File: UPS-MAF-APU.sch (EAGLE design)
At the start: 3 parts, among them J1 CONNECTOR_PI_40_PIN, J3 CONNECTOR_4, U1 OLED_I2C

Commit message: add more to-do items for schematic
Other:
- note added: "add battery/charger connector add INA260 add JST-4 for console add galvanic isolator add 1x6 for FTDI? add RJ-45 magjack add ENC28J60 eth IC package SS add power LED add OKI 78SR 5V SMPS add external temp connector add Si7006 internal temp/humidity add power, status lights"
- note removed: "add battery/charger connector add INA260 add JST-4 for console add 1x6 for FTDI? add RJ-45 magjack add ENC28J60 eth IC package SS add power LED add OKI 78SR 5V SMPS"
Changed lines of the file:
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@@
 add INA260
 add JST-4 for console
+add galvanic isolator
 add 1x6 for FTDI?
 add RJ-45 magjack
 add ENC28J60 eth IC package SS
 add power LED
-add OKI 78SR 5V SMPS</text>
+add OKI 78SR 5V SMPS
+add external temp connector
+add Si7006 internal temp/humidity
+add power, status lights</text>
 </plain>
 <instances>

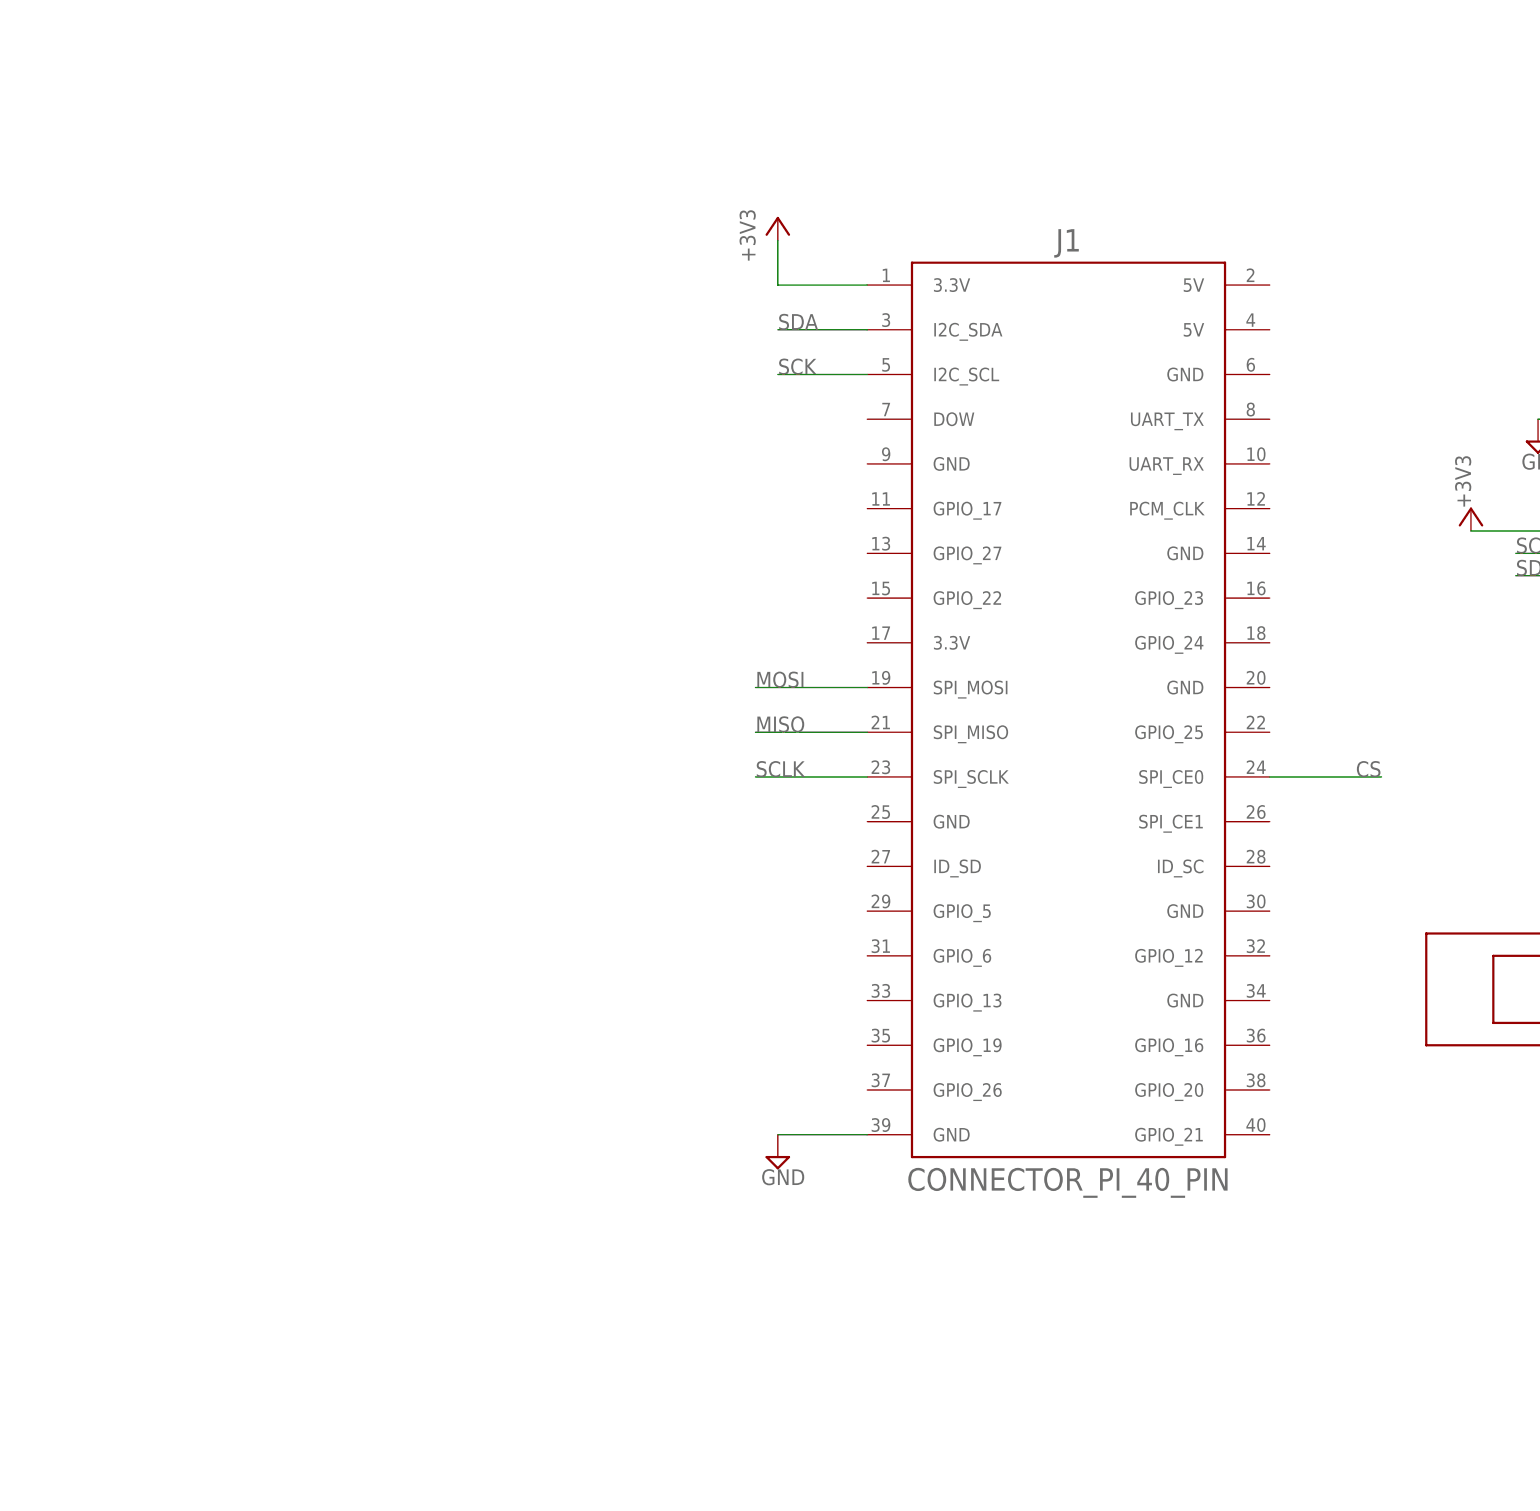
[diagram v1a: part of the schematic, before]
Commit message: Add parts to library, Schematic. Add barrel power jack, INA260 I/V sensor, 5V Murata SMPS.  Change parts to UPS library.
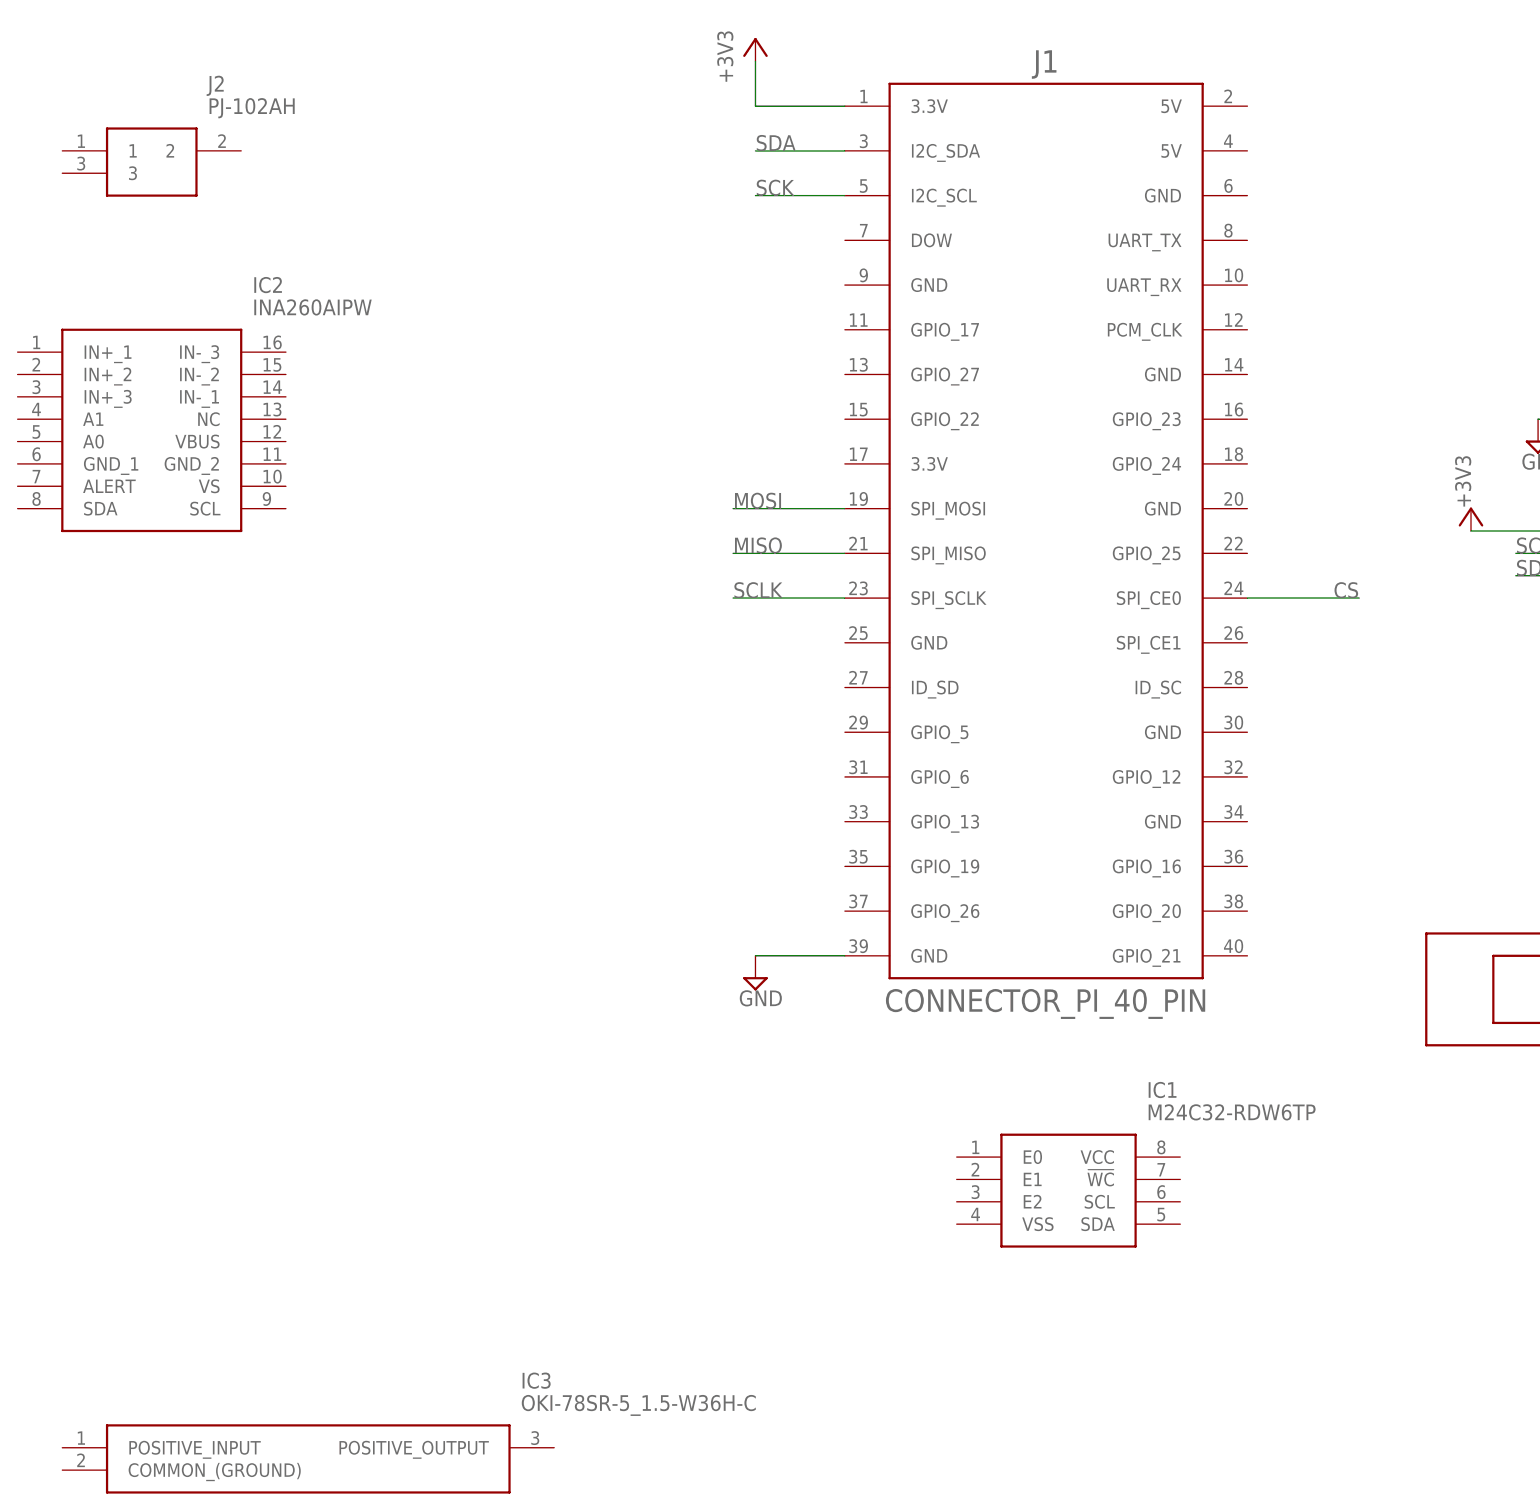
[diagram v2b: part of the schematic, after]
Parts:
- added IC1: M24C32-RDW6TP, APU_ENGR480_UPS_EAGLE_Library:M24C32-RDW6TP
- added IC2: INA260AIPW, APU_ENGR480_UPS_EAGLE_Library:INA260AIPW
- added IC3: OKI-78SR-5_1.5-W36H-C, APU_ENGR480_UPS_EAGLE_Library:OKI-78SR-5_1.5-W36H-C
- added J2: PJ-102AH, APU_ENGR480_UPS_EAGLE_Library:PJ-102AH
- J1: device ConnectBox_2019:CONNECTOR_PI_40_PIN -> APU_ENGR480_UPS_EAGLE_Library:CONNECTOR_PI_40_PIN
- J3: device ConnectBox_2019:CONNECTOR_4 -> APU_ENGR480_UPS_EAGLE_Library:CONNECTOR_4
- U1: device ConnectBox_2019:OLED_I2C -> APU_ENGR480_UPS_EAGLE_Library:OLED_I2C
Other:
- note added: "add battery/charger connector add JST-4 for console add galvanic isolator add 1x6 for FTDI? add RJ-45 magjack add power LED add external temp connector add Si7006 internal temp/humidity add power, status lights"
- note removed: "add battery/charger connector add INA260 add JST-4 for console add galvanic isolator add 1x6 for FTDI? add RJ-45 magjack add ENC28J60 eth IC package SS add power LED add OKI 78SR 5V SMPS add external temp connector add Si7006 internal temp/humidity add power, status lights"
- moved on the sheet: J1
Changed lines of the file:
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@@
 </classes>
 <parts>
-<part name="FRAME1" library="ConnectBox_2019" deviceset="FRAMES_LETTER_L" device=""/>
-<part name="J1" library="ConnectBox_2019" deviceset="CONNECTOR_PI_40_PIN" device=""/>
-<part name="+3V1" library="ConnectBox_2019" deviceset="+3V3" device=""/>
-<part name="SUPPLY2" library="ConnectBox_2019" deviceset="GND" device=""/>
-<part name="U1" library="ConnectBox_2019" deviceset="OLED_I2C" device=""/>
-<part name="+3V3" library="ConnectBox_2019" deviceset="+3V3" device=""/>
-<part name="SUPPLY3" library="ConnectBox_2019" deviceset="GND" device=""/>
-<part name="J3" library="ConnectBox_2019" deviceset="CONNECTOR_4" device=""/>
+<part name="FRAME1" library="APU_ENGR480_UPS_EAGLE_Library" deviceset="FRAMES_LETTER_L" device=""/>
+<part name="J1" library="APU_ENGR480_UPS_EAGLE_Library" deviceset="CONNECTOR_PI_40_PIN" device=""/>
+<part name="+3V1" library="APU_ENGR480_UPS_EAGLE_Library" deviceset="+3V3" device=""/>
+<part name="SUPPLY2" library="APU_ENGR480_UPS_EAGLE_Library" deviceset="GND" device=""/>
+<part name="U1" library="APU_ENGR480_UPS_EAGLE_Library" deviceset="OLED_I2C" device=""/>
+<part name="+3V3" library="APU_ENGR480_UPS_EAGLE_Library" deviceset="+3V3" device=""/>
+<part name="SUPPLY3" library="APU_ENGR480_UPS_EAGLE_Library" deviceset="GND" device=""/>
+<part name="J3" library="APU_ENGR480_UPS_EAGLE_Library" deviceset="CONNECTOR_4" device=""/>
+<part name="IC1" library="APU_ENGR480_UPS_EAGLE_Library" deviceset="M24C32-RDW6TP" device=""/>
+<part name="IC2" library="APU_ENGR480_UPS_EAGLE_Library" deviceset="INA260AIPW" device=""/>
+<part name="IC3" library="APU_ENGR480_UPS_EAGLE_Library" deviceset="OKI-78SR-5_1.5-W36H-C" device=""/>
+<part name="J2" library="APU_ENGR480_UPS_EAGLE_Library" deviceset="PJ-102AH" device=""/>
 </parts>
 <sheets>
@@
 <plain>
 <text x="-2.54" y="185.42" size="3.81" layer="88" align="top-right">add battery/charger connector
-add INA260
 add JST-4 for console
 add galvanic isolator
 add 1x6 for FTDI?
 add RJ-45 magjack
-add ENC28J60 eth IC package SS
 add power LED
-add OKI 78SR 5V SMPS
 add external temp connector
 add Si7006 internal temp/humidity
@@
 <attribute name="DRAWING_NAME" x="165.1" y="19.05" size="2.54" layer="94"/>
 </instance>
-<instance part="J1" gate="G$1" x="147.32" y="101.6" smashed="yes">
-<attribute name="NAME" x="147.32" y="154.94" size="2.54" layer="95" align="center"/>
-<attribute name="VALUE" x="147.32" y="48.26" size="2.54" layer="96" align="center"/>
+<instance part="J1" gate="G$1" x="144.78" y="121.92" smashed="yes">
+<attribute name="NAME" x="144.78" y="175.26" size="2.54" layer="95" align="center"/>
+<attribute name="VALUE" x="144.78" y="68.58" size="2.54" layer="96" align="center"/>
 </instance>
-<instance part="+3V1" gate="G$1" x="114.3" y="157.48" smashed="yes">
-<attribute name="VALUE" x="111.76" y="152.4" size="1.778" layer="96" rot="R90"/>
+<instance part="+3V1" gate="G$1" x="111.76" y="177.8" smashed="yes">
+<attribute name="VALUE" x="109.22" y="172.72" size="1.778" layer="96" rot="R90"/>
 </instance>
-<instance part="SUPPLY2" gate="GND" x="114.3" y="50.8" smashed="yes">
-<attribute name="VALUE" x="112.395" y="47.625" size="1.778" layer="96"/>
+<instance part="SUPPLY2" gate="GND" x="111.76" y="71.12" smashed="yes">
+<attribute name="VALUE" x="109.855" y="67.945" size="1.778" layer="96"/>
 </instance>
 <instance part="U1" gate="G$1" x="213.36" y="71.12" smashed="yes">
@@
 <attribute name="NAME" x="218.44" y="129.54" size="2.0828" layer="95" rot="MR180" align="center"/>
 </instance>
+<instance part="IC1" gate="G$1" x="134.62" y="50.8" smashed="yes">
+<attribute name="NAME" x="156.21" y="58.42" size="1.778" layer="95" align="center-left"/>
+<attribute name="VALUE" x="156.21" y="55.88" size="1.778" layer="96" align="center-left"/>
+</instance>
+<instance part="IC2" gate="G$1" x="27.94" y="142.24" smashed="yes">
+<attribute name="NAME" x="54.61" y="149.86" size="1.778" layer="95" align="center-left"/>
+<attribute name="VALUE" x="54.61" y="147.32" size="1.778" layer="96" align="center-left"/>
+</instance>
+<instance part="IC3" gate="G$1" x="33.02" y="17.78" smashed="yes">
+<attribute name="NAME" x="85.09" y="25.4" size="1.778" layer="95" align="center-left"/>
+<attribute name="VALUE" x="85.09" y="22.86" size="1.778" layer="96" align="center-left"/>
+</instance>
+<instance part="J2" gate="G$1" x="33.02" y="165.1" smashed="yes">
+<attribute name="NAME" x="49.53" y="172.72" size="1.778" layer="95" align="center-left"/>
+<attribute name="VALUE" x="49.53" y="170.18" size="1.778" layer="96" align="center-left"/>
+</instance>
 </instances>
 <busses>
@@
 <segment>
 <pinref part="J1" gate="G$1" pin="SPI_CE0@24"/>
-<wire x1="182.88" y1="93.98" x2="170.18" y2="93.98" width="0.1524" layer="91"/>
-<label x="182.88" y="93.98" size="1.778" layer="95" rot="MR0"/>
+<wire x1="180.34" y1="114.3" x2="167.64" y2="114.3" width="0.1524" layer="91"/>
+<label x="180.34" y="114.3" size="1.778" layer="95" rot="MR0"/>
 </segment>
 </net>
@@
 <segment>
 <pinref part="J1" gate="G$1" pin="SPI_MOSI@19"/>
-<wire x1="111.76" y1="104.14" x2="124.46" y2="104.14" width="0.1524" layer="91"/>
-<label x="111.76" y="104.14" size="1.778" layer="95"/>
+<wire x1="109.22" y1="124.46" x2="121.92" y2="124.46" width="0.1524" layer="91"/>
+<label x="109.22" y="124.46" size="1.778" layer="95"/>
 </segment>
 </net>
@@
 <pinref part="J1" gate="G$1" pin="3.3V@1"/>
 <pinref part="+3V1" gate="G$1" pin="+3V3"/>
-<wire x1="114.3" y1="154.94" x2="114.3" y2="149.86" width="0.1524" layer="91"/>
-<wire x1="114.3" y1="149.86" x2="124.46" y2="149.86" width="0.1524" layer="91"/>
+<wire x1="111.76" y1="175.26" x2="111.76" y2="170.18" width="0.1524" layer="91"/>
+<wire x1="111.76" y1="170.18" x2="121.92" y2="170.18" width="0.1524" layer="91"/>
 </segment>
 <segment>
@@
 <pinref part="J1" gate="G$1" pin="GND@39"/>
 <pinref part="SUPPLY2" gate="GND" pin="GND"/>
-<wire x1="114.3" y1="53.34" x2="124.46" y2="53.34" width="0.1524" layer="91"/>
+<wire x1="111.76" y1="73.66" x2="121.92" y2="73.66" width="0.1524" layer="91"/>
 </segment>
 <segment>
@@
 <segment>
 <pinref part="J1" gate="G$1" pin="SPI_SCLK@23"/>
-<wire x1="111.76" y1="93.98" x2="124.46" y2="93.98" width="0.1524" layer="91"/>
-<label x="111.76" y="93.98" size="1.778" layer="95"/>
+<wire x1="109.22" y1="114.3" x2="121.92" y2="114.3" width="0.1524" layer="91"/>
+<label x="109.22" y="114.3" size="1.778" layer="95"/>
 </segment>
 </net>
@@
 <segment>
 <pinref part="J1" gate="G$1" pin="SPI_MISO@21"/>
-<wire x1="111.76" y1="99.06" x2="124.46" y2="99.06" width="0.1524" layer="91"/>
-<label x="111.76" y="99.06" size="1.778" layer="95"/>
+<wire x1="109.22" y1="119.38" x2="121.92" y2="119.38" width="0.1524" layer="91"/>
+<label x="109.22" y="119.38" size="1.778" layer="95"/>
 </segment>
 </net>
@@
 <segment>
 <pinref part="J1" gate="G$1" pin="I2C_SCL@5"/>
-<wire x1="124.46" y1="139.7" x2="114.3" y2="139.7" width="0.1524" layer="91"/>
-<label x="114.3" y="139.7" size="1.778" layer="95"/>
+<wire x1="121.92" y1="160.02" x2="111.76" y2="160.02" width="0.1524" layer="91"/>
+<label x="111.76" y="160.02" size="1.778" layer="95"/>
 </segment>
 </net>
@@
 <segment>
 <pinref part="J1" gate="G$1" pin="I2C_SDA@3"/>
-<wire x1="114.3" y1="144.78" x2="124.46" y2="144.78" width="0.1524" layer="91"/>
-<label x="114.3" y="144.78" size="1.778" layer="95"/>
+<wire x1="111.76" y1="165.1" x2="121.92" y2="165.1" width="0.1524" layer="91"/>
+<label x="111.76" y="165.1" size="1.778" layer="95"/>
 </segment>
 </net>
